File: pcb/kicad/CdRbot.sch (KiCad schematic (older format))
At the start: 9 parts

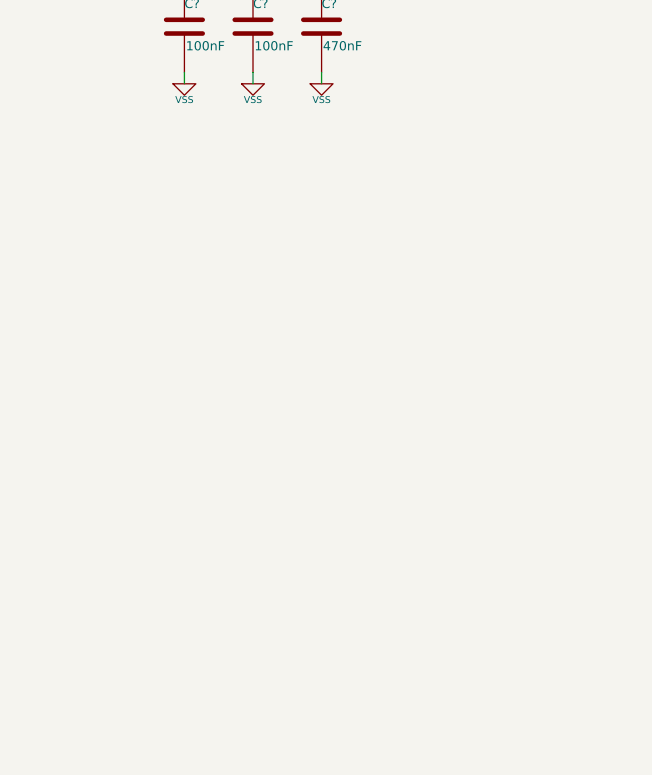
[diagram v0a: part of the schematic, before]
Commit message: Modifications to the schematic
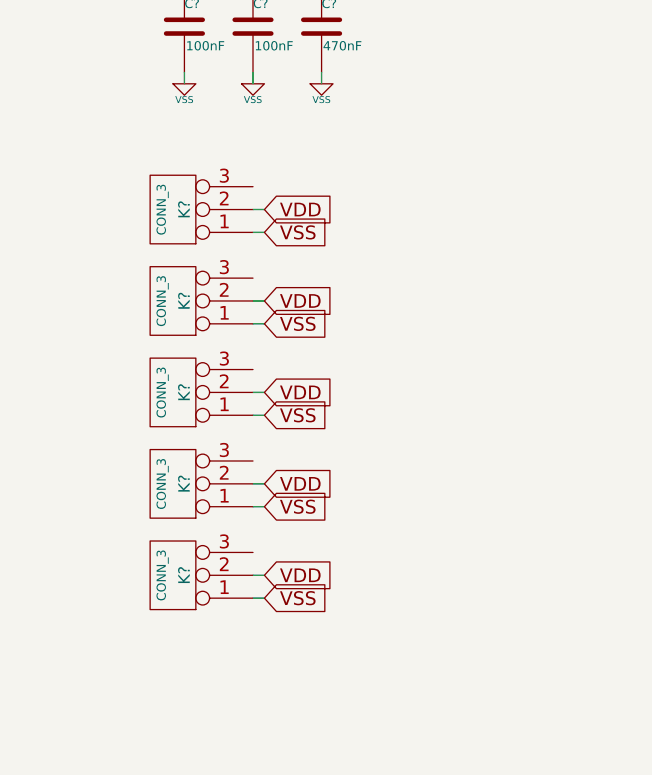
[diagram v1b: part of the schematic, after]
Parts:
- added K? (x5): CONN_3, ~, symbol CONN_3
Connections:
- net VDD: now also K?.2 (PM), K?.2 (PM), K?.2 (PM), K?.2 (PM), K?.2 (PM)
- net VSS: now also K?.1 (P1), K?.1 (P1), K?.1 (P1), K?.1 (P1), K?.1 (P1)
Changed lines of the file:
@@
-EESchema Schematic File Version 2  date Fri 03 May 2013 12:40:44 AM PYT
+EESchema Schematic File Version 2  date Fri 03 May 2013 04:10:01 PM PYT
 LIBS:power
 LIBS:device
@@
 LIBS:contrib
 LIBS:valves
+LIBS:CdRbot-cache
 EELAYER 24 0
 EELAYER END
@@
 Wire Wire Line
 	1950 2850 1950 2900
+$Comp
+L CONN_3 K?
+U 1 1 51841825
+P 1300 3450
+F 0 "K?" V 1250 3450 50  0000 C CNN
+F 1 "CONN_3" V 1350 3450 40  0000 C CNN
+F 2 "~" H 1300 3450 60  0000 C CNN
+F 3 "~" H 1300 3450 60  0000 C CNN
+	1    1300 3450
+	-1   0    0    1
+$EndComp
+Text GLabel 1700 3450 2    60   Input ~ 0
+VDD
+Text GLabel 1700 3550 2    60   Input ~ 0
+VSS
+Wire Wire Line
+	1650 3450 1700 3450
+Wire Wire Line
+	1700 3550 1650 3550
+$Comp
+L CONN_3 K?
+U 1 1 518418CD
+P 1300 3850
+F 0 "K?" V 1250 3850 50  0000 C CNN
+F 1 "CONN_3" V 1350 3850 40  0000 C CNN
+F 2 "~" H 1300 3850 60  0000 C CNN
+F 3 "~" H 1300 3850 60  0000 C CNN
+	1    1300 3850
+	-1   0    0    1
+$EndComp
+Text GLabel 1700 3850 2    60   Input ~ 0
+VDD
+Text GLabel 1700 3950 2    60   Input ~ 0
+VSS
+Wire Wire Line
+	1650 3850 1700 3850
+Wire Wire Line
+	1700 3950 1650 3950
+$Comp
+L CONN_3 K?
+U 1 1 518418D7
+P 1300 4650
+F 0 "K?" V 1250 4650 50  0000 C CNN
+F 1 "CONN_3" V 1350 4650 40  0000 C CNN
+F 2 "~" H 1300 4650 60  0000 C CNN
+F 3 "~" H 1300 4650 60  0000 C CNN
+	1    1300 4650
+	-1   0    0    1
+$EndComp
+Text GLabel 1700 4650 2    60   Input ~ 0
+VDD
+Text GLabel 1700 4750 2    60   Input ~ 0
+VSS
+Wire Wire Line
+	1650 4650 1700 4650
+Wire Wire Line
+	1700 4750 1650 4750
+$Comp
+L CONN_3 K?
+U 1 1 518418E1
+P 1300 4250
+F 0 "K?" V 1250 4250 50  0000 C CNN
+F 1 "CONN_3" V 1350 4250 40  0000 C CNN
+F 2 "~" H 1300 4250 60  0000 C CNN
+F 3 "~" H 1300 4250 60  0000 C CNN
+	1    1300 4250
+	-1   0    0    1
+$EndComp
+Text GLabel 1700 4250 2    60   Input ~ 0
+VDD
+Text GLabel 1700 4350 2    60   Input ~ 0
+VSS
+Wire Wire Line
+	1650 4250 1700 4250
+Wire Wire Line
+	1700 4350 1650 4350
+$Comp
+L CONN_3 K?
+U 1 1 518418EB
+P 1300 5050
+F 0 "K?" V 1250 5050 50  0000 C CNN
+F 1 "CONN_3" V 1350 5050 40  0000 C CNN
+F 2 "~" H 1300 5050 60  0000 C CNN
+F 3 "~" H 1300 5050 60  0000 C CNN
+	1    1300 5050
+	-1   0    0    1
+$EndComp
+Text GLabel 1700 5050 2    60   Input ~ 0
+VDD
+Text GLabel 1700 5150 2    60   Input ~ 0
+VSS
+Wire Wire Line
+	1650 5050 1700 5050
+Wire Wire Line
+	1700 5150 1650 5150
 $EndSCHEMATC

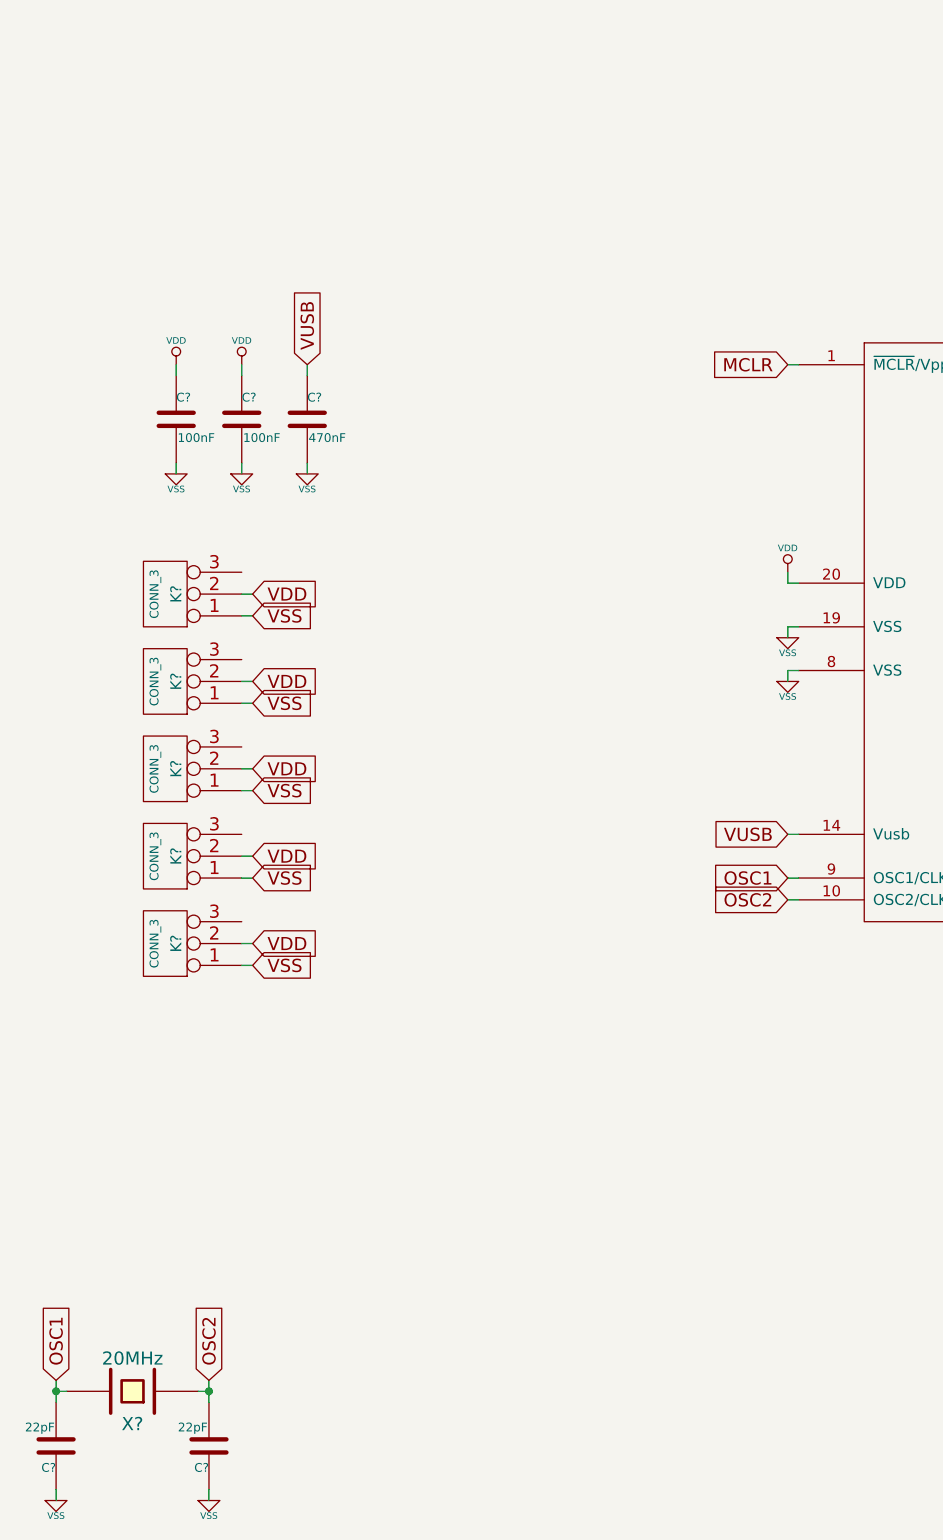
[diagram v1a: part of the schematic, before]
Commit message: Agregando archivos Kicad
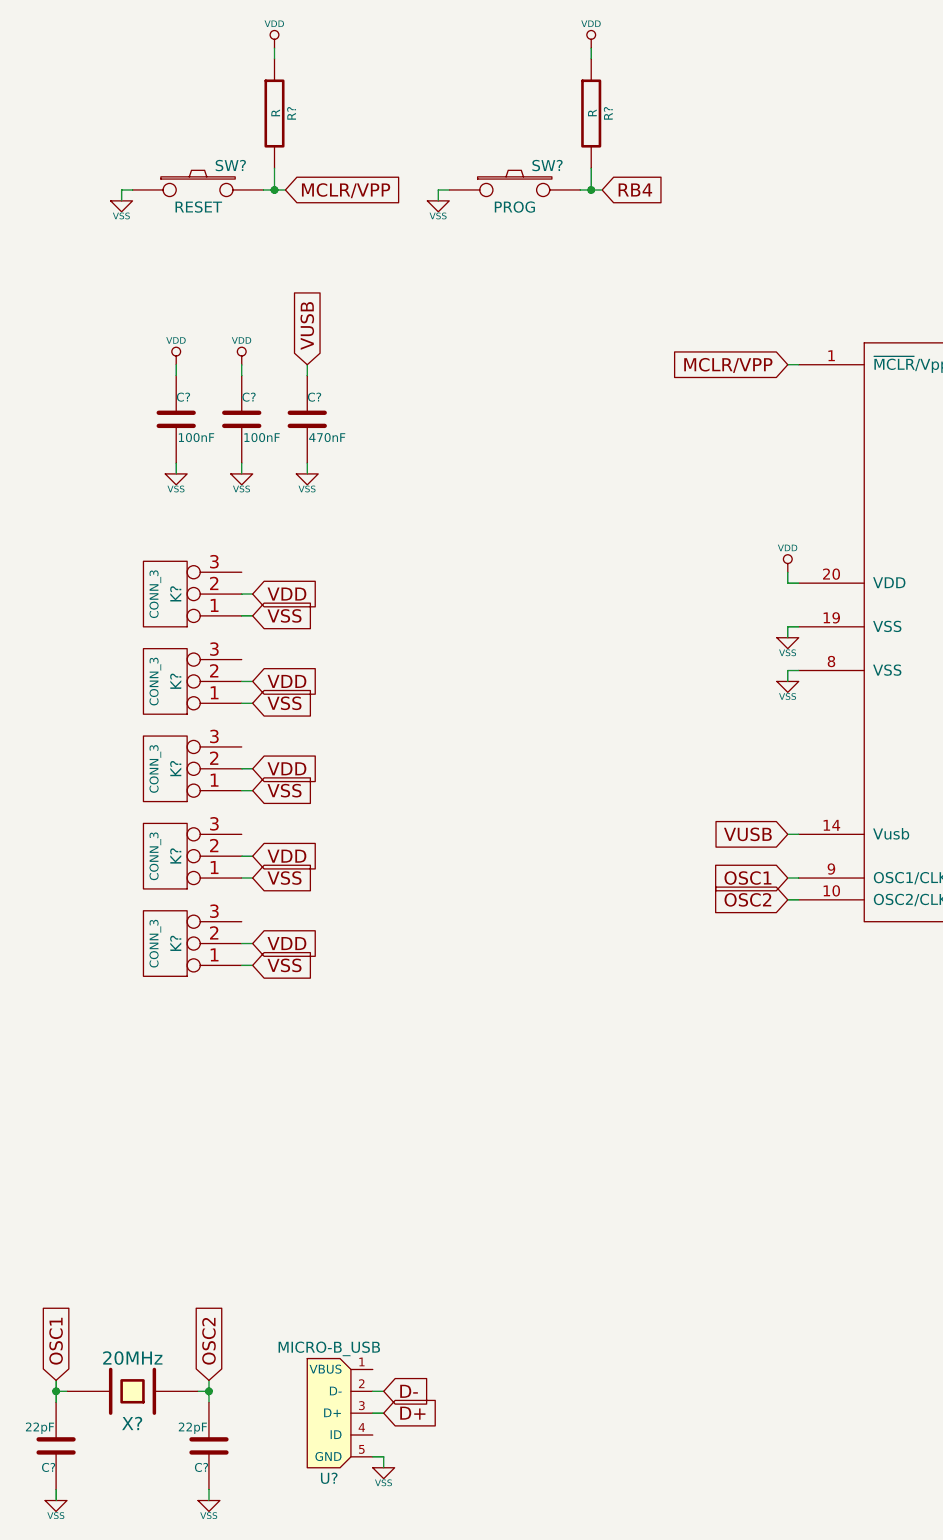
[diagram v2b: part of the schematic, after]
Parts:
- added R? (x2): R, ~, symbol R
- added SW?: RESET, ~, symbol SW_PUSH
- added SW?: PROG, ~, symbol SW_PUSH
- added U?: MICRO-B_USB, ~, symbol MICRO-B_USB
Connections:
- net D+: now also U?.3 (D+)
- net D-: now also U?.2 (D-)
- net VDD: now also R?.1, R?.1
- net VSS: now also SW?.1, SW?.1, U?.5 (GND)
- net MCLR renamed MCLR/VPP
- net MCLR/VPP: now also R?.2, SW?.2
- new net RB4: R?.2, SW?.2
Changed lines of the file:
@@
-EESchema Schematic File Version 2  date Fri 03 May 2013 04:10:01 PM PYT
+EESchema Schematic File Version 2  date Fri 03 May 2013 06:52:44 PM PYT
 LIBS:power
 LIBS:device
@@
 LIBS:contrib
 LIBS:valves
+LIBS:open-project
 LIBS:CdRbot-cache
 EELAYER 24 0
@@
 Connection ~ 800  7100
 Text GLabel 4150 2400 0    60   Input ~ 0
-MCLR
+MCLR/VPP
 Text GLabel 4150 4750 0    60   Input ~ 0
 OSC1
@@
 Wire Wire Line
 	1700 5150 1650 5150
+$Comp
+L MICRO-B_USB U?
+U 1 1 5184322D
+P 2050 7200
+F 0 "U?" H 2050 6900 50  0000 C CNN
+F 1 "MICRO-B_USB" H 2050 7500 50  0000 C CNN
+F 2 "~" H 2050 7200 60  0000 C CNN
+F 3 "~" H 2050 7200 60  0000 C CNN
+	1    2050 7200
+	1    0    0    -1
+$EndComp
+Text GLabel 2300 7100 2    60   Input ~ 0
+D-
+Text GLabel 2300 7200 2    60   Input ~ 0
+D+
+$Comp
+L VSS #PWR?
+U 1 1 5184323C
+P 2300 7450
+F 0 "#PWR?" H 2300 7450 30  0001 C CNN
+F 1 "VSS" H 2300 7380 30  0000 C CNN
+F 2 "" H 2300 7450 60  0000 C CNN
+F 3 "" H 2300 7450 60  0000 C CNN
+	1    2300 7450
+	1    0    0    -1
+$EndComp
+Wire Wire Line
+	2250 7100 2300 7100
+Wire Wire Line
+	2300 7200 2250 7200
+Wire Wire Line
+	2250 7400 2300 7400
+Wire Wire Line
+	2300 7400 2300 7450
+$Comp
+L SW_PUSH SW?
+U 1 1 51843DBA
+P 1450 1600
+F 0 "SW?" H 1600 1710 50  0000 C CNN
+F 1 "RESET" H 1450 1520 50  0000 C CNN
+F 2 "~" H 1450 1600 60  0000 C CNN
+F 3 "~" H 1450 1600 60  0000 C CNN
+	1    1450 1600
+	1    0    0    -1
+$EndComp
+$Comp
+L SW_PUSH SW?
+U 1 1 51843DCD
+P 2900 1600
+F 0 "SW?" H 3050 1710 50  0000 C CNN
+F 1 "PROG" H 2900 1520 50  0000 C CNN
+F 2 "~" H 2900 1600 60  0000 C CNN
+F 3 "~" H 2900 1600 60  0000 C CNN
+	1    2900 1600
+	1    0    0    -1
+$EndComp
+$Comp
+L R R?
+U 1 1 51843DDC
+P 1800 1250
+F 0 "R?" V 1880 1250 40  0000 C CNN
+F 1 "R" V 1807 1251 40  0000 C CNN
+F 2 "~" V 1730 1250 30  0000 C CNN
+F 3 "~" H 1800 1250 30  0000 C CNN
+	1    1800 1250
+	1    0    0    -1
+$EndComp
+$Comp
+L R R?
+U 1 1 51843DEB
+P 3250 1250
+F 0 "R?" V 3330 1250 40  0000 C CNN
+F 1 "R" V 3257 1251 40  0000 C CNN
+F 2 "~" V 3180 1250 30  0000 C CNN
+F 3 "~" H 3250 1250 30  0000 C CNN
+	1    3250 1250
+	1    0    0    -1
+$EndComp
+$Comp
+L VDD #PWR?
+U 1 1 51843E0E
+P 1800 950
+F 0 "#PWR?" H 1800 1050 30  0001 C CNN
+F 1 "VDD" H 1800 1060 30  0000 C CNN
+F 2 "" H 1800 950 60  0000 C CNN
+F 3 "" H 1800 950 60  0000 C CNN
+	1    1800 950
+	1    0    0    -1
+$EndComp
+$Comp
+L VDD #PWR?
+U 1 1 51843E1D
+P 3250 950
+F 0 "#PWR?" H 3250 1050 30  0001 C CNN
+F 1 "VDD" H 3250 1060 30  0000 C CNN
+F 2 "" H 3250 950 60  0000 C CNN
+F 3 "" H 3250 950 60  0000 C CNN
+	1    3250 950
+	1    0    0    -1
+$EndComp
+Wire Wire Line
+	1800 1000 1800 950
+Wire Wire Line
+	3200 1600 3300 1600
+Wire Wire Line
+	3250 1500 3250 1600
+Wire Wire Line
+	1800 1500 1800 1600
+Wire Wire Line
+	1750 1600 1850 1600
+Wire Wire Line
+	3250 950  3250 1000
+$Comp
+L VSS #PWR?
+U 1 1 518441C7
+P 2550 1650
+F 0 "#PWR?" H 2550 1650 30  0001 C CNN
+F 1 "VSS" H 2550 1580 30  0000 C CNN
+F 2 "" H 2550 1650 60  0000 C CNN
+F 3 "" H 2550 1650 60  0000 C CNN
+	1    2550 1650
+	1    0    0    -1
+$EndComp
+$Comp
+L VSS #PWR?
+U 1 1 518441E0
+P 1100 1650
+F 0 "#PWR?" H 1100 1650 30  0001 C CNN
+F 1 "VSS" H 1100 1580 30  0000 C CNN
+F 2 "" H 1100 1650 60  0000 C CNN
+F 3 "" H 1100 1650 60  0000 C CNN
+	1    1100 1650
+	1    0    0    -1
+$EndComp
+Wire Wire Line
+	1150 1600 1100 1600
+Wire Wire Line
+	1100 1600 1100 1650
+Wire Wire Line
+	2600 1600 2550 1600
+Wire Wire Line
+	2550 1600 2550 1650
+Text GLabel 1850 1600 2    60   Input ~ 0
+MCLR/VPP
+Connection ~ 1800 1600
+Text GLabel 3300 1600 2    60   Input ~ 0
+RB4
+Connection ~ 3250 1600
 $EndSCHEMATC
